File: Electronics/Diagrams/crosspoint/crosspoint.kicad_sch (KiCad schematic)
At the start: 0 parts

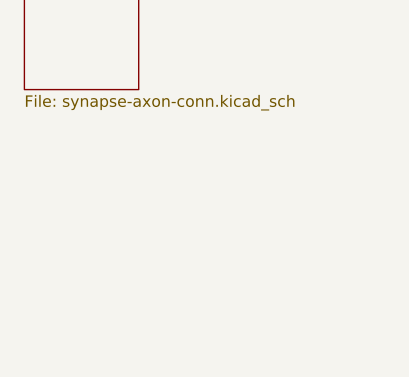
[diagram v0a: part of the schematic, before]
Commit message: Add images from svgs
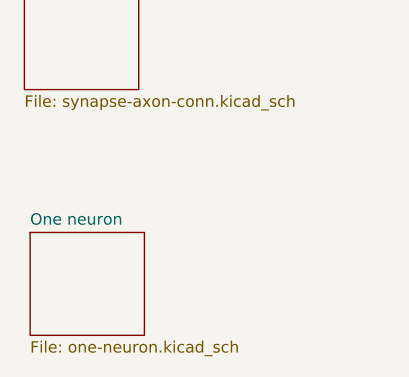
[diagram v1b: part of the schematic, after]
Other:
- added sheet One neuron (one-neuron.kicad_sch)
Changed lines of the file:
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@@
+    )
+  )
+  (sheet (at 39.37 83.82) (size 12.7 11.43) (fields_autoplaced)
+    (stroke (width 0.1524) (type solid))
+    (fill (color 0 0 0 0.0000))
+    (property "Sheetname" "One neuron" (at 39.37 83.1084 0)
+      (effects (font (size 1.27 1.27)) (justify left bottom))
+    )
+    (property "Sheetfile" "one-neuron.kicad_sch" (at 39.37 95.8346 0)
+      (effects (font (size 1.27 1.27)) (justify left top))
+    )
+    (instances
+      (project "crosspoint"
+        (path "/9024e212-450c-4133-b886-7ed6affd8f11" (page "4"))
+      )
     )
   )

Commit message: Now with added spelling...
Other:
- added sheet Scratchpad (scratchpad.kicad_sch)
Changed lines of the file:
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@@
+    )
+  )
+  (sheet (at 39.37 108.585) (size 12.7 11.43) (fields_autoplaced)
+    (stroke (width 0.1524) (type solid))
+    (fill (color 0 0 0 0.0000))
+    (property "Sheetname" "Scratchpad" (at 39.37 107.8734 0)
+      (effects (font (size 1.27 1.27)) (justify left bottom))
+    )
+    (property "Sheetfile" "scratchpad.kicad_sch" (at 39.37 120.5996 0)
+      (effects (font (size 1.27 1.27)) (justify left top))
+    )
+    (instances
+      (project "crosspoint"
+        (path "/9024e212-450c-4133-b886-7ed6affd8f11" (page "5"))
+      )
     )
   )
